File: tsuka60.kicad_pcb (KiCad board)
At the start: 2 copper layers, 285 x 95.1 mm, 177 parts, among them SW1 SW_Push, U1 ATmega32U4-AU, Y1 Resonator_Small

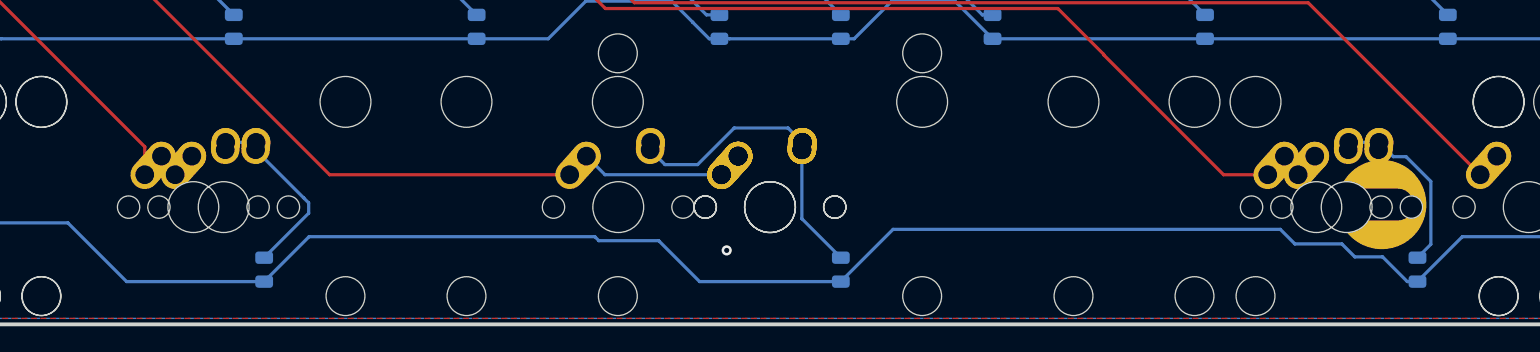
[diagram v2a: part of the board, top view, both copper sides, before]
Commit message: added two new 2.75u footprints for ALPS compatibility
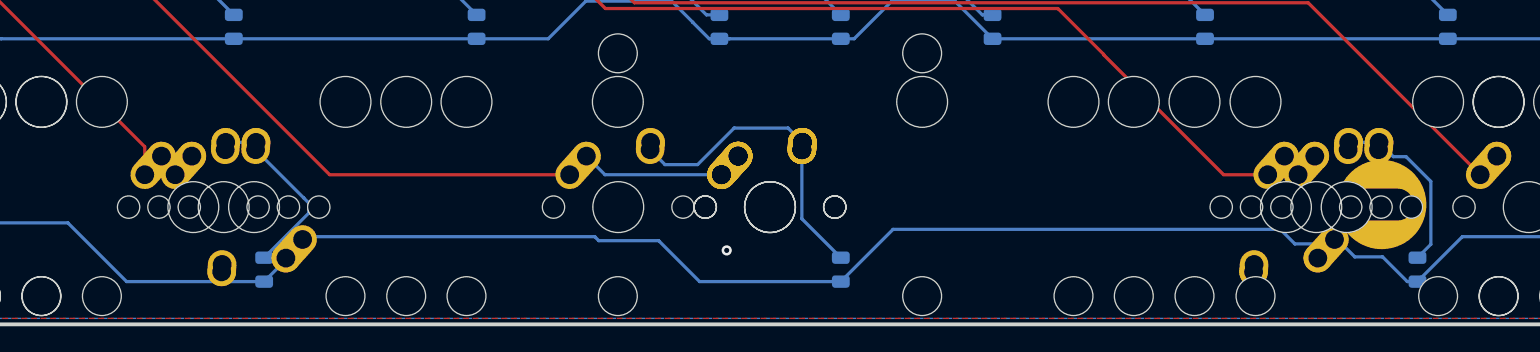
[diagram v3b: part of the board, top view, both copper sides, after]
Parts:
- added MX64-ALPS-1: SPACE LEFT, MX_Alps_Hybrid:MX-2.75U-NoLED, F.Cu at (196.8, 197.6)
- added MX66-ALPS-1: SPACE RIGHT, MX_Alps_Hybrid:MX-2.75U-NoLED, F.Cu at (277.8, 197.6)
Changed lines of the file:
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@@
     (tracks 1080)
     (zones 0)
-    (modules 177)
+    (modules 179)
     (nets 114)
   )
@@
     (pad "" np_thru_hole circle (at 5.08 0 48.0996) (size 1.75 1.75) (drill 1.75) (layers *.Cu *.Mask))
   )
+  (module MX_Alps_Hybrid:MX-2.75U-NoLED (layer F.Cu)
+    (at 196.85 197.64375 180)
+    (fp_text reference MX64-ALPS-1 (at 0 3.175) (layer Dwgs.User)
+      (effects (font (size 1 1) (thickness 0.15)))
+    )
+    (fp_text value "SPACE LEFT" (at 0 -7.9375) (layer Dwgs.User)
+      (effects (font (size 1 1) (thickness 0.15)))
+    )
+    (fp_line (start -26.19375 9.525) (end -26.19375 -9.525) (layer Dwgs.User) (width 0.15))
+    (fp_line (start -26.19375 9.525) (end 26.19375 9.525) (layer Dwgs.User) (width 0.15))
+    (fp_line (start 26.19375 -9.525) (end 26.19375 9.525) (layer Dwgs.User) (width 0.15))
+    (fp_line (start -26.19375 -9.525) (end 26.19375 -9.525) (layer Dwgs.User) (width 0.15))
+    (fp_line (start -7 -7) (end -7 -5) (layer Dwgs.User) (width 0.15))
+    (fp_line (start -5 -7) (end -7 -7) (layer Dwgs.User) (width 0.15))
+    (fp_line (start -7 7) (end -5 7) (layer Dwgs.User) (width 0.15))
+    (fp_line (start -7 5) (end -7 7) (layer Dwgs.User) (width 0.15))
+    (fp_line (start 7 7) (end 7 5) (layer Dwgs.User) (width 0.15))
+    (fp_line (start 5 7) (end 7 7) (layer Dwgs.User) (width 0.15))
+    (fp_line (start 7 -7) (end 7 -5) (layer Dwgs.User) (width 0.15))
+    (fp_line (start 5 -7) (end 7 -7) (layer Dwgs.User) (width 0.15))
+    (pad "" np_thru_hole circle (at 11.938 8.255 180) (size 3.9878 3.9878) (drill 3.9878) (layers *.Cu *.Mask))
+    (pad "" np_thru_hole circle (at -11.938 8.255 180) (size 3.9878 3.9878) (drill 3.9878) (layers *.Cu *.Mask))
+    (pad "" np_thru_hole circle (at 11.938 -6.985 180) (size 3.048 3.048) (drill 3.048) (layers *.Cu *.Mask))
+    (pad "" np_thru_hole circle (at -11.938 -6.985 180) (size 3.048 3.048) (drill 3.048) (layers *.Cu *.Mask))
+    (pad "" np_thru_hole circle (at 5.08 0 228.0996) (size 1.75 1.75) (drill 1.75) (layers *.Cu *.Mask))
+    (pad "" np_thru_hole circle (at -5.08 0 228.0996) (size 1.75 1.75) (drill 1.75) (layers *.Cu *.Mask))
+    (pad 1 thru_hole circle (at -2.5 -4 180) (size 2.25 2.25) (drill 1.47) (layers *.Cu B.Mask)
+      (net 82 Col3))
+    (pad "" np_thru_hole circle (at 0 0 180) (size 3.9878 3.9878) (drill 3.9878) (layers *.Cu *.Mask))
+    (pad 1 thru_hole oval (at -3.81 -2.54 228.0996) (size 4.211556 2.25) (drill 1.47 (offset 0.980778 0)) (layers *.Cu B.Mask)
+      (net 82 Col3))
+    (pad 2 thru_hole circle (at 2.54 -5.08 180) (size 2.25 2.25) (drill 1.47) (layers *.Cu B.Mask)
+      (net 68 "Net-(D64-Pad2)"))
+    (pad 2 thru_hole oval (at 2.5 -4.5 266.0548) (size 2.831378 2.25) (drill 1.47 (offset 0.290689 0)) (layers *.Cu B.Mask)
+      (net 68 "Net-(D64-Pad2)"))
+  )
+  (module MX_Alps_Hybrid:MX-2.75U-NoLED (layer F.Cu)
+    (at 277.8125 197.64375 180)
+    (fp_text reference MX66-ALPS-1 (at 0 3.175) (layer Dwgs.User)
+      (effects (font (size 1 1) (thickness 0.15)))
+    )
+    (fp_text value "SPACE RIGHT" (at 0 -7.9375) (layer Dwgs.User)
+      (effects (font (size 1 1) (thickness 0.15)))
+    )
+    (fp_line (start 5 -7) (end 7 -7) (layer Dwgs.User) (width 0.15))
+    (fp_line (start 7 -7) (end 7 -5) (layer Dwgs.User) (width 0.15))
+    (fp_line (start 5 7) (end 7 7) (layer Dwgs.User) (width 0.15))
+    (fp_line (start 7 7) (end 7 5) (layer Dwgs.User) (width 0.15))
+    (fp_line (start -7 5) (end -7 7) (layer Dwgs.User) (width 0.15))
+    (fp_line (start -7 7) (end -5 7) (layer Dwgs.User) (width 0.15))
+    (fp_line (start -5 -7) (end -7 -7) (layer Dwgs.User) (width 0.15))
+    (fp_line (start -7 -7) (end -7 -5) (layer Dwgs.User) (width 0.15))
+    (fp_line (start -26.19375 -9.525) (end 26.19375 -9.525) (layer Dwgs.User) (width 0.15))
+    (fp_line (start 26.19375 -9.525) (end 26.19375 9.525) (layer Dwgs.User) (width 0.15))
+    (fp_line (start -26.19375 9.525) (end 26.19375 9.525) (layer Dwgs.User) (width 0.15))
+    (fp_line (start -26.19375 9.525) (end -26.19375 -9.525) (layer Dwgs.User) (width 0.15))
+    (pad 2 thru_hole oval (at 2.5 -4.5 266.0548) (size 2.831378 2.25) (drill 1.47 (offset 0.290689 0)) (layers *.Cu B.Mask)
+      (net 111 "Net-(D66-Pad2)"))
+    (pad 2 thru_hole circle (at 2.54 -5.08 180) (size 2.25 2.25) (drill 1.47) (layers *.Cu B.Mask)
+      (net 111 "Net-(D66-Pad2)"))
+    (pad 1 thru_hole oval (at -3.81 -2.54 228.0996) (size 4.211556 2.25) (drill 1.47 (offset 0.980778 0)) (layers *.Cu B.Mask)
+      (net 84 Col5))
+    (pad "" np_thru_hole circle (at 0 0 180) (size 3.9878 3.9878) (drill 3.9878) (layers *.Cu *.Mask))
+    (pad 1 thru_hole circle (at -2.5 -4 180) (size 2.25 2.25) (drill 1.47) (layers *.Cu B.Mask)
+      (net 84 Col5))
+    (pad "" np_thru_hole circle (at -5.08 0 228.0996) (size 1.75 1.75) (drill 1.75) (layers *.Cu *.Mask))
+    (pad "" np_thru_hole circle (at 5.08 0 228.0996) (size 1.75 1.75) (drill 1.75) (layers *.Cu *.Mask))
+    (pad "" np_thru_hole circle (at -11.938 -6.985 180) (size 3.048 3.048) (drill 3.048) (layers *.Cu *.Mask))
+    (pad "" np_thru_hole circle (at 11.938 -6.985 180) (size 3.048 3.048) (drill 3.048) (layers *.Cu *.Mask))
+    (pad "" np_thru_hole circle (at -11.938 8.255 180) (size 3.9878 3.9878) (drill 3.9878) (layers *.Cu *.Mask))
+    (pad "" np_thru_hole circle (at 11.938 8.255 180) (size 3.9878 3.9878) (drill 3.9878) (layers *.Cu *.Mask))
+  )
   (gr_text "Tsuka60 aka Semi Ergo Layout\nPrototype Two\nby RominRonin" (at 127.762 131.064) (layer B.SilkS)
     (effects (font (size 1.016 1.016) (thickness 0.254)) (justify right mirror))
@@
   (segment (start 349.5375 146.3375) (end 349.2165 146.3375) (width 0.254) (layer B.Cu) (net 21))
   (segment (start 357.1875 146.3375) (end 349.5375 146.3375) (width 0.254) (layer B.Cu) (net 21))
+  (segment (start 125.57125 136.68375) (end 125.57125 136.74725) (width 0.254) (layer F.Cu) (net 22))
+  (segment (start 125.53125 141.40625) (end 128.5875 144.4625) (width 0.254) (layer B.Cu) (net 22))
+  (segment (start 125.53125 135.99375) (end 125.53125 141.40625) (width 0.254) (layer B.Cu) (net 22))
   (segment (start 144.58125 141.40625) (end 147.6375 144.4625) (width 0.254) (layer B.Cu) (net 23))
   (segment (start 144.58125 135.99375) (end 144.58125 141.40625) (width 0.254) (layer B.Cu) (net 23))
@@
   (segment (start 335.08125 141.40625) (end 338.1375 144.4625) (width 0.254) (layer B.Cu) (net 33))
   (segment (start 335.08125 135.99375) (end 335.08125 141.40625) (width 0.254) (layer B.Cu) (net 33))
-  (segment (start 347.13125 137.99375) (end 347.13125 136.99275) (width 0.254) (layer B.Cu) (net 92))
+  (segment (start 354.17125 141.44625) (end 354.17125 135.41375) (width 0.254) (layer B.Cu) (net 34))
+  (segment (start 357.1875 144.4625) (end 354.17125 141.44625) (width 0.254) (layer B.Cu) (net 34))
   (segment (start 373.18125 141.40625) (end 376.2375 144.4625) (width 0.254) (layer B.Cu) (net 35))
   (segment (start 373.18125 135.99375) (end 373.18125 141.40625) (width 0.254) (layer B.Cu) (net 35))
@@
   (segment (start 128.799999 192.518751) (end 127.675 193.64375) (width 0.254) (layer F.Cu) (net 80))
   (segment (start 128.74625 176.05375) (end 128.799999 176.107499) (width 0.254) (layer F.Cu) (net 80))
-  (segment (start 125.57125 136.68375) (end 125.57125 136.74725) (width 0.254) (layer F.Cu) (net 22))
-  (segment (start 125.53125 141.40625) (end 128.5875 144.4625) (width 0.254) (layer B.Cu) (net 22))
-  (segment (start 125.53125 135.99375) (end 125.53125 141.40625) (width 0.254) (layer B.Cu) (net 22))
-  (segment (start 354.17125 141.44625) (end 354.17125 135.41375) (width 0.254) (layer B.Cu) (net 34))
-  (segment (start 357.1875 144.4625) (end 354.17125 141.44625) (width 0.254) (layer B.Cu) (net 34))
   (segment (start 133.440751 171.359249) (end 128.74625 176.05375) (width 0.254) (layer F.Cu) (net 80))
   (segment (start 133.440751 159.167249) (end 133.440751 171.359249) (width 0.254) (layer F.Cu) (net 80))
@@
   (segment (start 327.65502 148.35502) (end 334.84375 155.54375) (width 0.254) (layer B.Cu) (net 91))
   (segment (start 156.650575 148.35502) (end 327.65502 148.35502) (width 0.254) (layer B.Cu) (net 91))
+  (segment (start 347.13125 137.99375) (end 347.13125 136.99275) (width 0.254) (layer B.Cu) (net 92))
   (segment (start 359.72401 154.46375) (end 361.315 154.46375) (width 0.254) (layer F.Cu) (net 92))
   (segment (start 358.742288 154.46375) (end 359.72401 154.46375) (width 0.254) (layer F.Cu) (net 92))

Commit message: removed lots of compatibility
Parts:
- removed MX37: LEGACY-H, MX_Alps_Hybrid:MX-1U-NoLED
- removed MX65-3: SPACE, MX_Alps_Hybrid:MX-6.25U-ReversedStabilizers-NoLED
- removed MX67-3: LEGACY-BOTTOM, MX_Alps_Hybrid:MX-1.25U-NoLED
- moved D64 7.14 mm to (190.5, 202.6)
- moved D38 4.76 mm to (242.9, 164.4)
- moved D66 3.97 mm to (284.2, 202.6)
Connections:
- MX38 pad 1: Net-(D38-Pad2) -> Col7
- MX38 pad 2: Col7 -> Net-(D38-Pad2)
- MX64-ALPS-1 pad 1: Col3 -> Net-(D64-Pad2)
- MX64-ALPS-1 pad 2: Net-(D64-Pad2) -> Col3
- MX66-ALPS-1 pad 1: Col5 -> Net-(D66-Pad2)
- MX66-ALPS-1 pad 2: Net-(D66-Pad2) -> Col5
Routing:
- net Col6: track 268.6 -> 190.0 mm
- net Col3: track 208.2 -> 230.7 mm
- net Col5: track 325.0 -> 340.1 mm
- net Net-(D65-Pad2): track 23.8 -> 9.73 mm
- net Net-(D64-Pad2): track 14.2 -> 26.6 mm
- net Net-(D67-Pad2): track 12.1 -> 0.00 mm
- net Net-(D38-Pad2): track 21.8 -> 12.1 mm
- net Col1: track 112.1 -> 118.3 mm
- net Net-(D66-Pad2): track 14.6 -> 20.3 mm
- net Row2: track 263.2 -> 265.9 mm
- net Col8: track 308.7 -> 310.7 mm
- net Row1: track 294.8 -> 293.7 mm
- net Col7: track 207.3 -> 208.5 mm
- net Row4: track 357.7 -> 358.7 mm
- net Col4: track 215.7 -> 216.4 mm

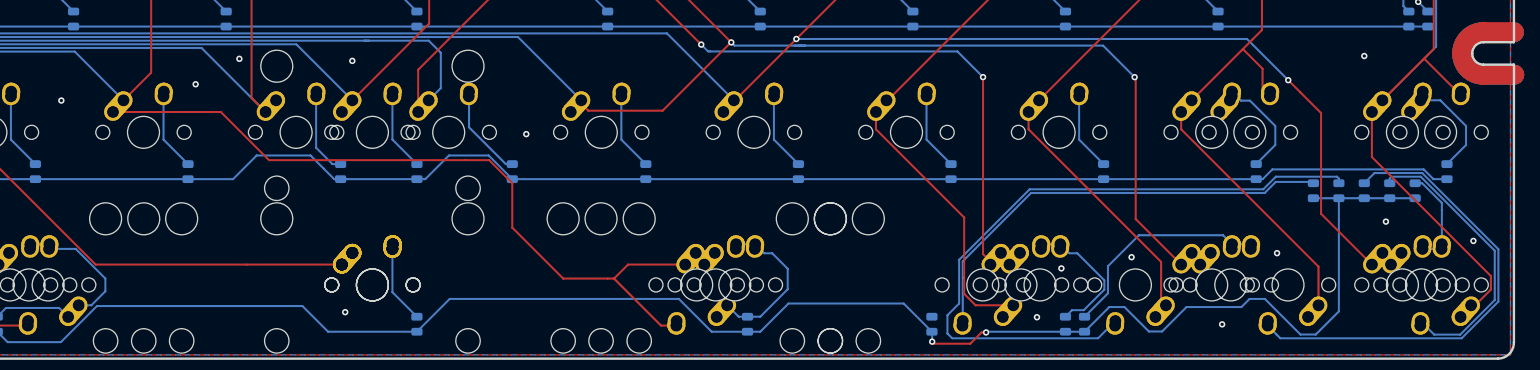
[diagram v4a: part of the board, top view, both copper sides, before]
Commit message: Adjusted bottom row. Need to add a new bottom row for the Colemak Forum people.
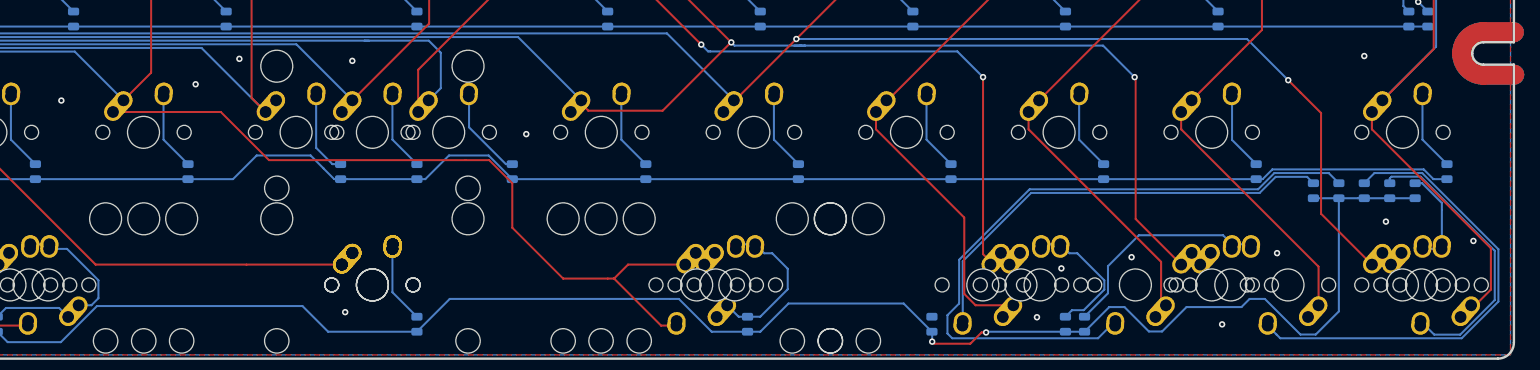
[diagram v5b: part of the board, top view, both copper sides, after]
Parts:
- removed MX59-1: SLASH, MX_Alps_Hybrid:MX-1.5U-NoLED
- removed MX60-1: R-SHIFT, MX_Alps_Hybrid:MX-1U-NoLED
- renumbered MX64-ALPS-1 to MX64-ALPS-4, MX66-ALPS-1 to MX66-ALPS-4
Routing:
- net Col13: track 367.6 -> 360.3 mm
- net Col14: track 392.0 -> 385.4 mm
- net Net-(D60-Pad2): track 12.8 -> 9.73 mm
- net Net-(D59-Pad2): track 12.9 -> 10.3 mm
- net Net-(D64-Pad2): track 26.6 -> 25.2 mm

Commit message: restructured the bottom rows
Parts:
- removed MX64-1: SPACE LEFT, MX_Alps_Hybrid:MX-2.75U-ReversedStabilizers-NoLED
- removed MX64-2: SPACE LEFT, MX_Alps_Hybrid:MX-3U-ReversedStabilizers-NoLED
- removed MX64-ALPS-4: SPACE LEFT, MX_Alps_Hybrid:MX-2.75U-NoLED
- removed MX65: SPACE, MX_Alps_Hybrid:MX-7U-ReversedStabilizers-NoLED
- removed MX66-1: SPACE RIGHT, MX_Alps_Hybrid:MX-2.75U-ReversedStabilizers-NoLED
- removed MX66-2: SPACE RIGHT, MX_Alps_Hybrid:MX-3U-ReversedStabilizers-NoLED
- removed MX66-ALPS-4: SPACE RIGHT, MX_Alps_Hybrid:MX-2.75U-NoLED
- removed MX69: R-ALT, MX_Alps_Hybrid:MX-1.5U-NoLED
- removed MX69-1: R-ALT, MX_Alps_Hybrid:MX-1.25U-NoLED
- removed MX70: R-WIN, MX_Alps_Hybrid:MX-1U-NoLED
- removed MX70-1: R-WIN, MX_Alps_Hybrid:MX-1.25U-NoLED
- removed MX71: R-CTRL, MX_Alps_Hybrid:MX-1.5U-NoLED
- removed MX72-4: LEFT, MX_Alps_Hybrid:MX-1U-NoLED
- removed MX73-4: DOWN, MX_Alps_Hybrid:MX-1U-NoLED
- removed MX74-4: UP, MX_Alps_Hybrid:MX-1U-NoLED
- removed MX75-4: RIGHT, MX_Alps_Hybrid:MX-1U-NoLED
- added D68: D_Small, Diode_SMD:D_0805_2012Metric, B.Cu at (54.0, 273.5)
- added MX61-3: FN, MX_Alps_Hybrid:MX-1U-NoLED, F.Cu at (104.8, 311.1)
- added MX62-3: CONTROL, MX_Alps_Hybrid:MX-1U-NoLED, F.Cu at (123.8, 311.1)
- added MX63-3: OPTION, MX_Alps_Hybrid:MX-1U-NoLED, F.Cu at (142.9, 311.1)
- added MX64-3: CMD, MX_Alps_Hybrid:MX-1U-NoLED, F.Cu at (161.9, 311.1)
- added MX65-3: LEFT SPACE, MX_Alps_Hybrid:MX-2.75U-ReversedStabilizers-NoLED, F.Cu at (197.6, 311.1)
- added MX65-4: CMD, MX_Alps_Hybrid:MX-1U-NoLED, F.Cu at (181.0, 335.8)
- added MX65-5: CMD, MX_Alps_Hybrid:MX-1.25U-NoLED, F.Cu at (183.4, 358.8)
- added MX66-4: LEFT SPACE, MX_Alps_Hybrid:MX-2U-ReversedStabilizers-NoLED, F.Cu at (209.6, 335.8)
- added MX66-5: LEFT SPACE, MX_Alps_Hybrid:MX-1.25U-NoLED, F.Cu at (207.2, 358.8)
- added MX67-5: LEFT CENTRE, MX_Alps_Hybrid:MX-1U-NoLED, F.Cu at (228.6, 358.8)
- added MX68: SPACE, MX_Alps_Hybrid:MX-7U-ReversedStabilizers-NoLED, F.Cu at (238.1, 231.8)
- added MX68-1: RETURN, MX_Alps_Hybrid:MX-2U-ReversedStabilizers-NoLED, F.Cu at (238.1, 261.1)
- added MX69-5: RIGHT CENTRE, MX_Alps_Hybrid:MX-1U-NoLED, F.Cu at (247.7, 358.8)
- added MX70-4: RIGHT SPACE, MX_Alps_Hybrid:MX-2U-ReversedStabilizers-NoLED, F.Cu at (266.7, 335.8)
- added MX70-5: RIGHT SPACE, MX_Alps_Hybrid:MX-1.25U-NoLED, F.Cu at (269.1, 358.8)
- added MX71-2: RIGHT SPACE, MX_Alps_Hybrid:MX-3U-ReversedStabilizers-NoLED, F.Cu at (281.0, 287.3)
- added MX71-3: RIGHT SPACE, MX_Alps_Hybrid:MX-2.75U-ReversedStabilizers-NoLED, F.Cu at (278.6, 311.1)
- added MX71-4: CMD, MX_Alps_Hybrid:MX-1U-NoLED, F.Cu at (295.3, 335.8)
- added MX71-5: CMD, MX_Alps_Hybrid:MX-1.25U-NoLED, F.Cu at (292.9, 358.8)
- added MX72-3: LEFT, MX_Alps_Hybrid:MX-1U-NoLED, F.Cu at (314.3, 311.1)
- added MX73: R-ALT, MX_Alps_Hybrid:MX-1.5U-NoLED, F.Cu at (319.1, 231.8)
- added MX73-1: R-ALT, MX_Alps_Hybrid:MX-1.25U-NoLED, F.Cu at (321.5, 261.1)
- added MX73-3: DOWN, MX_Alps_Hybrid:MX-1U-NoLED, F.Cu at (333.4, 311.1)
- added MX74: R-WIN, MX_Alps_Hybrid:MX-1U-NoLED, F.Cu at (342.9, 231.8)
- added MX74-1: R-WIN, MX_Alps_Hybrid:MX-1.25U-NoLED, F.Cu at (345.3, 261.1)
- added MX74-3: UP, MX_Alps_Hybrid:MX-1U-NoLED, F.Cu at (352.4, 311.1)
- added MX75: R-CTRL, MX_Alps_Hybrid:MX-1.5U-NoLED, F.Cu at (366.7, 231.8)
- added MX75-1: R-CTRL, MX_Alps_Hybrid:MX-1.25U-NoLED, F.Cu at (369.1, 261.1)
- added MX75-3: RIGHT, MX_Alps_Hybrid:MX-1U-NoLED, F.Cu at (371.5, 311.1)
- MX65-1: value RETURN -> LEFT SPACE; footprint MX_Alps_Hybrid:MX-2U-ReversedStabilizers-NoLED -> MX_Alps_Hybrid:MX-2.75U-ReversedStabilizers-NoLED
- MX65-2: value RETURN -> LEFT SPACE; footprint MX_Alps_Hybrid:MX-1.5U-NoLED -> MX_Alps_Hybrid:MX-3U-ReversedStabilizers-NoLED
- MX71-1: value R-CTRL -> RIGHT SPACE; footprint MX_Alps_Hybrid:MX-1.25U-NoLED -> MX_Alps_Hybrid:MX-2.75U-ReversedStabilizers-NoLED
- moved D70 283.7 mm to (54.0, 282.4)
- moved D69 280.2 mm to (54.0, 278.0)
- moved D67 271.2 mm to (46.2, 276.1)
- moved D66 247.8 mm to (46.2, 271.6)
- moved D65 207.1 mm to (46.2, 267.2)
- moved D64 151.9 mm to (54.0, 269.1)
- moved D63 130.5 mm to (46.2, 262.7)
- moved D61 111.0 mm to (43.7, 288.1)
- moved MX71-1 106.0 mm to (283.4, 261.1)
- moved D62 104.6 mm to (54.0, 264.6)
- moved MX65-2 99.1 mm to (195.3, 287.3)
- moved MX65-1 77.5 mm to (192.9, 261.1)
- moved MX61-1 63.5 mm to (107.2, 261.1)
- moved MX62-1 63.5 mm to (131.0, 261.1)
- moved MX63-1 63.5 mm to (154.8, 261.1)
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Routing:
- net Row4: track 358.7 -> 62.4 mm, vias 2 -> 0
- net Col4: track 216.4 -> 161.8 mm
- net Net-(D74-Pad2): track 59.1 -> 7.76 mm
- net Col3: track 230.7 -> 184.5 mm
- net Net-(D73-Pad2): track 84.3 -> 40.0 mm
- net Col5: track 340.1 -> 297.2 mm
- net Net-(D75-Pad2): track 35.5 -> 4.55 mm
- net Col14: track 385.4 -> 355.9 mm
- net Col13: track 360.3 -> 331.3 mm
- net Col12: track 314.4 -> 285.3 mm
- net Net-(D70-Pad2): track 27.9 -> 0.00 mm
- net Col9: track 322.8 -> 295.2 mm
- net Col8: track 310.7 -> 284.5 mm
- net Net-(D64-Pad2): track 25.2 -> 0.00 mm
- net Col2: track 177.9 -> 153.6 mm
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
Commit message: Traced routes for the new layouts, improved much of the other tracing
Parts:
- MX65-3, MX71-3: footprint MX_Alps_Hybrid:MX-2.75U-ReversedStabilizers-NoLED -> MX_Alps_Hybrid:MX-2.75U-NoLED
- moved D70 205.8 mm to (243.7, 202.6)
- moved D69 200.5 mm to (239.7, 202.6)
- moved D67 198.9 mm to (231.0, 202.6)
- moved D68 194.4 mm to (234.9, 202.6)
- moved MX65-5 161.1 mm to (182.6, 197.6)
- moved MX66-5 161.1 mm to (206.4, 197.6)
- moved MX67-5 161.1 mm to (227.8, 197.6)
- moved MX69-5 161.1 mm to (246.9, 197.6)
- moved MX70-5 161.1 mm to (268.3, 197.6)
- moved MX71-5 161.1 mm to (292.1, 197.6)
- moved D65 141.0 mm to (171.4, 202.6)
- moved D66 139.6 mm to (167.5, 202.6)
- moved MX65-4 138.1 mm to (180.2, 197.6)
- moved MX66-4 138.1 mm to (208.8, 197.6)
- moved MX70-4 138.1 mm to (265.9, 197.6)
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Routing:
- net Row4: track 62.4 -> 350.4 mm
- net Net-(D71-Pad2): track 5.22 -> 127.7 mm
- net Col4: track 161.8 -> 228.7 mm
- net Col14: track 355.9 -> 422.6 mm
- net Net-(D66-Pad2): track 0.00 -> 63.1 mm
- net Net-(D65-Pad2): track 0.00 -> 61.7 mm, vias 0 -> 1
- net Net-(D74-Pad2): track 7.76 -> 68.2 mm
- net Net-(D75-Pad2): track 4.55 -> 62.0 mm
- net Col1: track 99.5 -> 149.9 mm
- net Col12: track 285.3 -> 332.1 mm
- net Col8: track 284.5 -> 239.5 mm, vias 2 -> 0
- net Col13: track 331.3 -> 376.1 mm
- net Net-(D72-Pad2): track 36.4 -> 79.6 mm
- net Col9: track 295.2 -> 255.2 mm, vias 2 -> 0
- net Net-(D63-Pad2): track 0.00 -> 39.9 mm
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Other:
- board text added: "Tsuka60 Prototype Three by RominRonin"
- board text removed: "Tsuka60 aka Semi Ergo Layout Prototype Two by RominRonin"
